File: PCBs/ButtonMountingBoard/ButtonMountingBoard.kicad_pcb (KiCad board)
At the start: 2 copper layers, 223.5 x 19.1 mm, 34 parts, among them J1 Conn_01x06_Male, J2 Conn_01x10_Male, J3 Conn_01x06_Male, SW1 SW_TACT_LED, SW2 SW_TACT_LED, SW3 SW_TACT_LED, SW4 SW_TACT_LED, SW5 SW_TACT_LED, SW6 SW_TACT_LED, SW7 SW_TACT_LED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

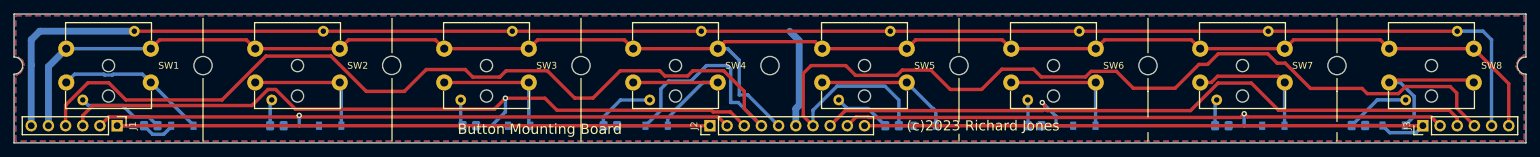
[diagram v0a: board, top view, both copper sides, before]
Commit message: V1.1 PCB updates after initial testing 1. Share data out line between LCD, 7 Segment and button scan to yield spare io lines for    control of WS8212 LEDs for music stand lamp 2. Replace level shifting FET on Button Driver PCBs by resistor 3. Generate combined ks61,button driver & button mount prototype PCB for economic testing with JLC PCB
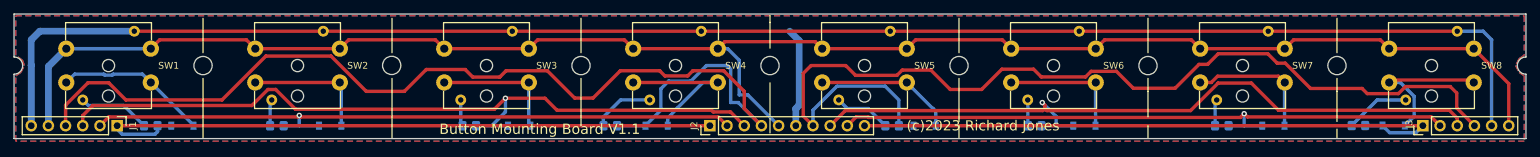
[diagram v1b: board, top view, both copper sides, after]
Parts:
- R1, R2, R3, R4, R5, R6, R7, R8: value 270 -> 560
- turned R1 to 0 degrees
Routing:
- net Net-(R1-Pad1): track 12.6 -> 10.6 mm
- net Net-(D1-Pad2): track 96.8 -> 97.5 mm
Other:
- board size 223.5 x 19.1 mm -> 223.5 x 18.4 mm
- board text added: "Button Mounting Board V1.1"
- board text added: "SW 0V SW5 SW6 SW7 SW8"
- board text added: "SW1 SW2 SW3 SW4 SW 0V"
- board text removed: "Button Mounting Board"
- board text removed: "LED SW SW5 SW6 SW7 SW8"
- board text removed: "SW1 SW2 SW3 SW4 SW LED"
